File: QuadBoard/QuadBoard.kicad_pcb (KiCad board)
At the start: 2 copper layers, 62.2 x 48.9 mm, 8 parts, among them J1 Conn_01x06_Pin, U1 ESP32-S3-DevKitC

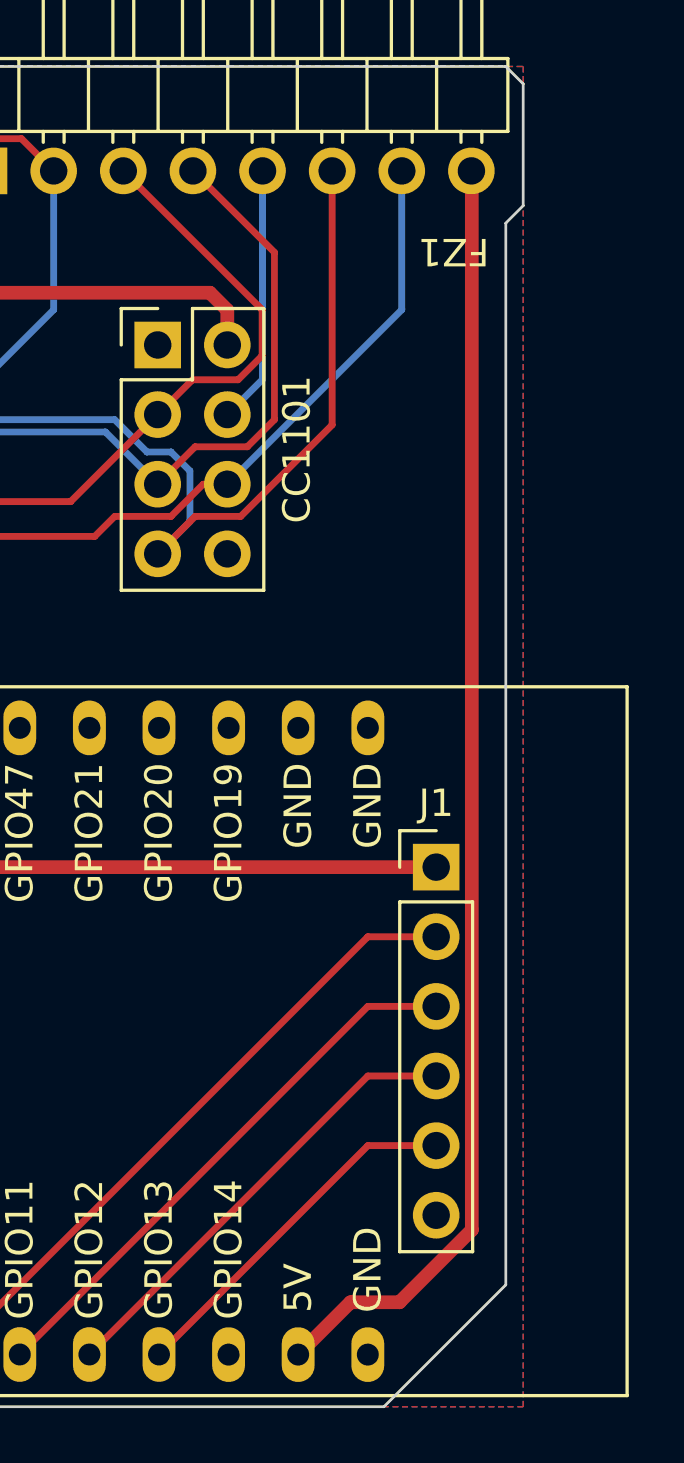
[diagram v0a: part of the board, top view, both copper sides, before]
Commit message: Update SD footprint
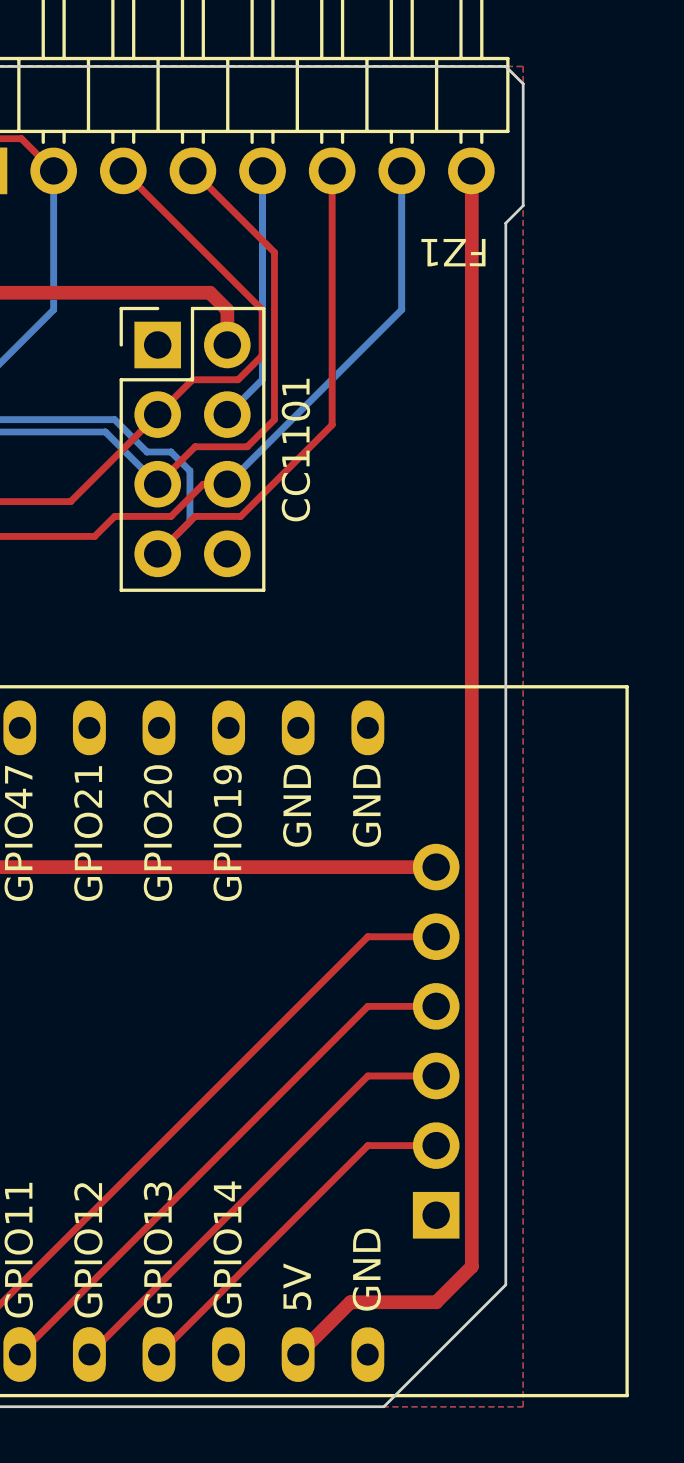
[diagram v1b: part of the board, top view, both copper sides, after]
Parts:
- removed J1: Conn_01x06_Pin, Connector_PinHeader_2.54mm:PinHeader_1x06_P2.54mm_Vertical
- added U2: ~, FlipperLibrary:SD, B.Cu at (190.5, 88.9)
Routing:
- net +5V: track 46.9 -> 47.6 mm
